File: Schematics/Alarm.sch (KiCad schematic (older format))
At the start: 7 parts, among them U8 BluetoothModule, U9 Arduino

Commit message: Fixed a layer
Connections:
- wire segments 37 -> 36
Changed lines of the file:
@@
 	4050 2800 4050 3400
 Wire Wire Line
-	7450 3400 7400 3400
-Wire Wire Line
 	6000 3400 6000 3300
-Connection ~ 7400 3400
-Wire Wire Line
-	7400 3400 6000 3400
 Wire Wire Line
 	5950 3400 5950 3500
@@
 Wire Wire Line
 	5050 3200 5650 3200
+Wire Wire Line
+	6000 3400 7400 3400
 $EndSCHEMATC

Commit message: Fixed repo
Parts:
- removed U9: Arduino, symbol CapstoneSchematic:Arduino
- added XA?: Arduino_Mega2560_Shield, symbol CapstoneSchematic:Arduino_Mega2560_Shield
- renumbered Alarm_Silence1 to Alarm_Silence, BZ1 to BZ?, D_RED2 to D_RED?, R4 to R?, U8 to U?, ULoRa2 to ULoRa?
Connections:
- wire segments 36 -> 56
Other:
- moved on the sheet: Alarm_Silence, BZ?, D_RED?, R?, U?, ULoRa?

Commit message: Made things look better on wireless alarm
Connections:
- net +5V: no longer XA?.5V3 (5V)
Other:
- note removed: "From USB Adapter"
- note removed: "Wireless Alarm Schematic"
- moved on the sheet: Alarm_Silence, BZ?, D_RED?, R?, ULoRa?

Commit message: Added Michael's alarm pcb rev
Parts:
- Alarm_Silence1: renamed from Alarm_Silence; footprint (none) -> Button_Switch_THT:SW_PUSH_6mm
- BZ1: renamed from BZ?; footprint (none) -> Buzzer_Beeper:Buzzer_15x7.5RM7.6
- D_RED1: renamed from D_RED?; footprint (none) -> LED_THT:LED_D5.0mm
- R1: renamed from R?; footprint (none) -> Resistor_THT:R_Axial_DIN0207_L6.3mm_D2.5mm_P2.54mm_Vertical
- U1: renamed from U?; footprint (none) -> Connector_PinSocket_2.54mm:PinSocket_1x04_P2.54mm_Horizontal
- ULoRa1: renamed from ULoRa?; footprint (none) -> Connector_PinSocket_2.54mm:PinSocket_1x06_P2.54mm_Horizontal
- XA1: renamed from XA?; footprint (none) -> Arduino:Arduino_Mega2560_Shield
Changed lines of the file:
@@
 EESchema Schematic File Version 4
-LIBS:CapstoneSchematic-cache
+LIBS:Alarm-cache
 EELAYER 30 0
 EELAYER END
 $Descr A4 11693 8268
 encoding utf-8
-Sheet 2 2
+Sheet 1 1
 Title "Wireless Alarm Schematic"
 Date ""
@@
 $EndDescr
 $Comp
-L power:GND #PWR?
+L power:GND #PWR0101
 U 1 1 5DC5496C
 P 11000 1800
-AR Path="/5DC5496C" Ref="#PWR?"  Part="1"
+AR Path="/5DC5496C" Ref="#PWR0101"  Part="1"
 AR Path="/5DC4244F/5DC5496C" Ref="#PWR0122"  Part="1"
-F 0 "#PWR0122" H 11000 1550 50  0001 C CNN
+F 0 "#PWR0101" H 11000 1550 50  0001 C CNN
 F 1 "GND" H 11005 1627 50  0000 C CNN
 F 2 "" H 11000 1800 50  0001 C CNN
@@
 $EndComp
 $Comp
-L Device:R R?
+L Device:R R1
 U 1 1 5DC54972
 P 10450 1800
-AR Path="/5DC54972" Ref="R?"  Part="1"
+AR Path="/5DC54972" Ref="R1"  Part="1"
 AR Path="/5DC4244F/5DC54972" Ref="R?"  Part="1"
-F 0 "R?" H 10380 1754 50  0000 R CNN
+F 0 "R1" H 10380 1754 50  0000 R CNN
 F 1 "220" H 10380 1845 50  0000 R CNN
-F 2 "" V 10380 1800 50  0001 C CNN
+F 2 "Resistor_THT:R_Axial_DIN0207_L6.3mm_D2.5mm_P2.54mm_Vertical" V 10380 1800 50  0001 C CNN
 F 3 "~" H 10450 1800 50  0001 C CNN
 	1    10450 1800
@@
 $EndComp
 $Comp
-L power:GND #PWR?
+L power:GND #PWR0102
 U 1 1 5DC549DA
 P 4225 2825
-AR Path="/5DC549DA" Ref="#PWR?"  Part="1"
+AR Path="/5DC549DA" Ref="#PWR0102"  Part="1"
 AR Path="/5DC4244F/5DC549DA" Ref="#PWR0123"  Part="1"
-F 0 "#PWR0123" H 4225 2575 50  0001 C CNN
+F 0 "#PWR0102" H 4225 2575 50  0001 C CNN
 F 1 "GND" H 4230 2652 50  0000 C CNN
 F 2 "" H 4225 2825 50  0001 C CNN
@@
 $EndComp
 $Comp
-L power:+5V #PWR?
+L power:+5V #PWR0103
 U 1 1 5DC549E0
 P 4225 2325
-AR Path="/5DC549E0" Ref="#PWR?"  Part="1"
+AR Path="/5DC549E0" Ref="#PWR0103"  Part="1"
 AR Path="/5DC4244F/5DC549E0" Ref="#PWR0124"  Part="1"
-F 0 "#PWR0124" H 4225 2175 50  0001 C CNN
+F 0 "#PWR0103" H 4225 2175 50  0001 C CNN
 F 1 "+5V" H 4240 2498 50  0000 C CNN
 F 2 "" H 4225 2325 50  0001 C CNN
@@
 $EndComp
 $Comp
-L Device:LED D_RED?
+L Device:LED D_RED1
 U 1 1 5DC54A01
 P 10750 1800
-AR Path="/5DC54A01" Ref="D_RED?"  Part="1"
+AR Path="/5DC54A01" Ref="D_RED1"  Part="1"
 AR Path="/5DC4244F/5DC54A01" Ref="D_RED?"  Part="1"
-F 0 "D_RED?" H 10743 2016 50  0000 C CNN
+F 0 "D_RED1" H 10743 2016 50  0000 C CNN
 F 1 "LED" H 10743 1925 50  0000 C CNN
-F 2 "" H 10750 1800 50  0001 C CNN
+F 2 "LED_THT:LED_D5.0mm" H 10750 1800 50  0001 C CNN
 F 3 "~" H 10750 1800 50  0001 C CNN
 	1    10750 1800
@@
 	11000 1800 10900 1800
 $Comp
-L Device:Buzzer BZ?
+L Device:Buzzer BZ1
 U 1 1 5DC609D6
 P 10150 1225
-F 0 "BZ?" H 10156 900 50  0000 C CNN
+F 0 "BZ1" H 10156 900 50  0000 C CNN
 F 1 "Buzzer" H 10156 991 50  0000 C CNN
-F 2 "" V 10125 1325 50  0001 C CNN
+F 2 "Buzzer_Beeper:Buzzer_15x7.5RM7.6" V 10125 1325 50  0001 C CNN
 F 3 "~" V 10125 1325 50  0001 C CNN
 	1    10150 1225
@@
 $EndComp
 $Comp
-L power:GND #PWR?
+L power:GND #PWR0104
 U 1 1 5DC60A34
 P 10250 1125
-AR Path="/5DC60A34" Ref="#PWR?"  Part="1"
+AR Path="/5DC60A34" Ref="#PWR0104"  Part="1"
 AR Path="/5DC4244F/5DC60A34" Ref="#PWR0126"  Part="1"
-F 0 "#PWR0126" H 10250 875 50  0001 C CNN
+F 0 "#PWR0104" H 10250 875 50  0001 C CNN
 F 1 "GND" V 10255 997 50  0000 R CNN
 F 2 "" H 10250 1125 50  0001 C CNN
@@
 $EndComp
 $Comp
-L power:+5V #PWR?
+L power:+5V #PWR0105
 U 1 1 5DC69508
 P 4150 1800
-AR Path="/5DC69508" Ref="#PWR?"  Part="1"
+AR Path="/5DC69508" Ref="#PWR0105"  Part="1"
 AR Path="/5DC4244F/5DC69508" Ref="#PWR0128"  Part="1"
-F 0 "#PWR0128" H 4150 1650 50  0001 C CNN
+F 0 "#PWR0105" H 4150 1650 50  0001 C CNN
 F 1 "+5V" H 4165 1973 50  0000 C CNN
 F 2 "" H 4150 1800 50  0001 C CNN
@@
 $EndComp
 $Comp
-L power:GND #PWR?
+L power:GND #PWR0106
 U 1 1 5DC69FE6
 P 4150 2000
-AR Path="/5DC69FE6" Ref="#PWR?"  Part="1"
+AR Path="/5DC69FE6" Ref="#PWR0106"  Part="1"
 AR Path="/5DC4244F/5DC69FE6" Ref="#PWR0129"  Part="1"
-F 0 "#PWR0129" H 4150 1750 50  0001 C CNN
+F 0 "#PWR0106" H 4150 1750 50  0001 C CNN
 F 1 "GND" H 4155 1827 50  0000 C CNN
 F 2 "" H 4150 2000 50  0001 C CNN
@@
 11/1/2019
 $Comp
-L power:GND #PWR?
+L power:GND #PWR0107
 U 1 1 5E4A2B00
 P 6350 5000
-F 0 "#PWR?" H 6350 4750 50  0001 C CNN
+F 0 "#PWR0107" H 6350 4750 50  0001 C CNN
 F 1 "GND" H 6355 4827 50  0000 C CNN
 F 2 "" H 6350 5000 50  0001 C CNN
@@
 	9450 2100 9050 2100
 $Comp
-L CapstoneSchematic:LoRa ULoRa?
+L CapstoneSchematic:LoRa ULoRa1
 U 1 1 5DC549E8
 P 4125 2325
-AR Path="/5DC549E8" Ref="ULoRa?"  Part="1"
+AR Path="/5DC549E8" Ref="ULoRa1"  Part="1"
 AR Path="/5DC4244F/5DC549E8" Ref="ULoRa?"  Part="1"
-F 0 "ULoRa?" H 5503 2271 50  0000 L CNN
+F 0 "ULoRa1" H 5503 2271 50  0000 L CNN
 F 1 "LoRa" H 5503 2180 50  0000 L CNN
-F 2 "" H 4675 2125 50  0001 C CNN
+F 2 "Connector_PinSocket_2.54mm:PinSocket_1x06_P2.54mm_Horizontal" H 4675 2125 50  0001 C CNN
 F 3 "" H 4675 2125 50  0001 C CNN
 	1    4125 2325
@@
 $EndComp
 $Comp
-L CapstoneSchematic:BluetoothModule U?
+L CapstoneSchematic:BluetoothModule U1
 U 1 1 5DC67D77
 P 4050 1500
-F 0 "U?" H 4294 885 50  0000 C CNN
+F 0 "U1" H 4294 885 50  0000 C CNN
 F 1 "BluetoothModule" H 4294 976 50  0000 C CNN
-F 2 "" H 4350 1000 50  0001 C CNN
+F 2 "Connector_PinSocket_2.54mm:PinSocket_1x04_P2.54mm_Horizontal" H 4350 1000 50  0001 C CNN
 F 3 "" H 4350 1000 50  0001 C CNN
 	1    4050 1500
@@
 $EndComp
 $Comp
-L CapstoneSchematic:Arduino_Mega2560_Shield XA?
+L CapstoneSchematic:Arduino_Mega2560_Shield XA1
 U 1 1 5E49C0DD
 P 7750 3750
-F 0 "XA?" H 7750 1370 60  0000 C CNN
+F 0 "XA1" H 7750 1370 60  0000 C CNN
 F 1 "Arduino_Mega2560_Shield" H 7750 1264 60  0000 C CNN
-F 2 "" H 8450 6500 60  0001 C CNN
+F 2 "Arduino:Arduino_Mega2560_Shield" H 8450 6500 60  0001 C CNN
 F 3 "https://store.arduino.cc/arduino-mega-2560-rev3" H 8450 6500 60  0001 C CNN
 	1    7750 3750
@@
 $EndComp
 $Comp
-L power:+5V #PWR?
+L power:+5V #PWR0108
 U 1 1 5DC6E068
 P 10200 2425
-AR Path="/5DC6E068" Ref="#PWR?"  Part="1"
+AR Path="/5DC6E068" Ref="#PWR0108"  Part="1"
 AR Path="/5DC4244F/5DC6E068" Ref="#PWR0130"  Part="1"
-F 0 "#PWR0130" H 10200 2275 50  0001 C CNN
+F 0 "#PWR0108" H 10200 2275 50  0001 C CNN
 F 1 "+5V" H 10215 2598 50  0000 C CNN
 F 2 "" H 10200 2425 50  0001 C CNN
@@
 $EndComp
 $Comp
-L Switch:SW_MEC_5G Alarm_Silence
-U 1 1 5DC6DC68
-P 9925 2425
-F 0 "Alarm_Silence" H 9925 2710 50  0000 C CNN
-F 1 "SW_MEC_5G" H 9925 2619 50  0000 C CNN
-F 2 "" H 9925 2625 50  0001 C CNN
-F 3 "http://www.apem.com/int/index.php?controller=attachment&id_attachment=488" H 9925 2625 50  0001 C CNN
-	1    9925 2425
-	-1   0    0    -1
-$EndComp
-$Comp
-L power:+5V #PWR?
+L power:+5V #PWR0109
 U 1 1 5E54092B
 P 6350 5600
-F 0 "#PWR?" H 6350 5450 50  0001 C CNN
+F 0 "#PWR0109" H 6350 5450 50  0001 C CNN
 F 1 "+5V" H 6365 5773 50  0000 C CNN
 F 2 "" H 6350 5600 50  0001 C CNN
@@
 Wire Wire Line
 	9450 2425 9725 2425
+$Comp
+L Switch:SW_MEC_5G Alarm_Silence1
+U 1 1 5DC6DC68
+P 9925 2425
+F 0 "Alarm_Silence1" H 9925 2710 50  0000 C CNN
+F 1 "SW_MEC_5G" H 9925 2619 50  0000 C CNN
+F 2 "Button_Switch_THT:SW_PUSH_6mm" H 9925 2625 50  0001 C CNN
+F 3 "http://www.apem.com/int/index.php?controller=attachment&id_attachment=488" H 9925 2625 50  0001 C CNN
+	1    9925 2425
+	-1   0    0    -1
+$EndComp
 $EndSCHEMATC

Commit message: Fixed button
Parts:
- removed Alarm_Silence1: SW_MEC_5G, Button_Switch_THT:SW_PUSH_6mm, symbol Switch:SW_MEC_5G
- removed D_RED1: LED, LED_THT:LED_D5.0mm, symbol Device:LED
- removed R1: 220, Resistor_THT:R_Axial_DIN0207_L6.3mm_D2.5mm_P2.54mm_Vertical, symbol Device:R
- added SW?: SW_MEC_5G_LED, symbol Switch:SW_MEC_5G_LED
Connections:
- net GND: now also SW?.1, SW?.2
- net at XA1.D7: now also SW?.3 (K)
- net at XA1.D8: now also SW?.4 (A)
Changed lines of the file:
@@
 EESchema Schematic File Version 4
-LIBS:CapstoneSchematic-cache
+LIBS:Alarm-cache
 EELAYER 30 0
 EELAYER END
 $Descr A4 11693 8268
 encoding utf-8
-Sheet 1 2
+Sheet 1 1
 Title "Wireless Alarm Schematic"
 Date ""
@@
 Comment4 ""
 $EndDescr
-$Comp
-L power:GND #PWR0101
-U 1 1 5DC5496C
-P 11000 1800
-AR Path="/5DC5496C" Ref="#PWR0101"  Part="1"
-AR Path="/5DC4244F/5DC5496C" Ref="#PWR0122"  Part="1"
-F 0 "#PWR0101" H 11000 1550 50  0001 C CNN
-F 1 "GND" H 11005 1627 50  0000 C CNN
-F 2 "" H 11000 1800 50  0001 C CNN
-F 3 "" H 11000 1800 50  0001 C CNN
-	1    11000 1800
-	0    -1   -1   0
-$EndComp
-$Comp
-L Device:R R1
-U 1 1 5DC54972
-P 10450 1800
-AR Path="/5DC54972" Ref="R1"  Part="1"
-AR Path="/5DC4244F/5DC54972" Ref="R?"  Part="1"
-F 0 "R1" H 10380 1754 50  0000 R CNN
-F 1 "220" H 10380 1845 50  0000 R CNN
-F 2 "Resistor_THT:R_Axial_DIN0207_L6.3mm_D2.5mm_P2.54mm_Vertical" V 10380 1800 50  0001 C CNN
-F 3 "~" H 10450 1800 50  0001 C CNN
-	1    10450 1800
-	0    -1   -1   0
-$EndComp
 $Comp
 L power:GND #PWR0102
@@
 $EndComp
 $Comp
-L Device:LED D_RED1
-U 1 1 5DC54A01
-P 10750 1800
-AR Path="/5DC54A01" Ref="D_RED1"  Part="1"
-AR Path="/5DC4244F/5DC54A01" Ref="D_RED?"  Part="1"
-F 0 "D_RED1" H 10743 2016 50  0000 C CNN
-F 1 "LED" H 10743 1925 50  0000 C CNN
-F 2 "LED_THT:LED_D5.0mm" H 10750 1800 50  0001 C CNN
-F 3 "~" H 10750 1800 50  0001 C CNN
-	1    10750 1800
-	-1   0    0    -1
-$EndComp
-Wire Wire Line
-	11000 1800 10900 1800
-$Comp
 L Device:Buzzer BZ1
 U 1 1 5DC609D6
@@
 Wire Wire Line
 	4675 2425 4225 2425
-Text GLabel 9600 2000 2    50   Input ~ 0
-Lora_Reset
 Wire Wire Line
 	6450 1600 4150 1600
@@
 	9600 2000 9050 2000
 Wire Wire Line
-	9450 2100 9050 2100
+	9450 2200 9050 2200
 $Comp
 L CapstoneSchematic:LoRa ULoRa1
@@
 $EndComp
 $Comp
-L power:+5V #PWR0108
-U 1 1 5DC6E068
-P 10200 2425
-AR Path="/5DC6E068" Ref="#PWR0108"  Part="1"
-AR Path="/5DC4244F/5DC6E068" Ref="#PWR0130"  Part="1"
-F 0 "#PWR0108" H 10200 2275 50  0001 C CNN
-F 1 "+5V" H 10215 2598 50  0000 C CNN
-F 2 "" H 10200 2425 50  0001 C CNN
-F 3 "" H 10200 2425 50  0001 C CNN
-	1    10200 2425
-	0    1    -1   0
-$EndComp
-$Comp
 L power:+5V #PWR0109
 U 1 1 5E54092B
@@
 	6350 5600 6450 5600
 Wire Wire Line
-	9050 1800 10300 1800
-Wire Wire Line
 	9750 1100 10050 1100
 Wire Wire Line
@@
 	5400 1900 5400 2625
 Wire Wire Line
-	10125 2425 10200 2425
-Wire Wire Line
-	9450 2100 9450 2425
+	10125 2425 10150 2425
+Text GLabel 9600 2000 2    50   Input ~ 0
+Lora_Reset
+$Comp
+L Switch:SW_MEC_5G_LED SW?
+U 1 1 5E936E97
+P 9925 2325
+F 0 "SW?" H 9925 2710 50  0000 C CNN
+F 1 "SW_MEC_5G_LED" H 9925 2619 50  0000 C CNN
+F 2 "" H 9925 2625 50  0001 C CNN
+F 3 "http://www.apem.com/int/index.php?controller=attachment&id_attachment=488" H 9925 2625 50  0001 C CNN
+	1    9925 2325
+	-1   0    0    1
+$EndComp
+Wire Wire Line
+	10125 2325 10150 2325
+Wire Wire Line
+	10150 2325 10150 2425
+Connection ~ 10150 2425
+Wire Wire Line
+	10150 2425 10200 2425
+$Comp
+L power:GND #PWR?
+U 1 1 5E944770
+P 10200 2425
+F 0 "#PWR?" H 10200 2175 50  0001 C CNN
+F 1 "GND" V 10205 2297 50  0000 R CNN
+F 2 "" H 10200 2425 50  0001 C CNN
+F 3 "" H 10200 2425 50  0001 C CNN
+	1    10200 2425
+	0    -1   -1   0
+$EndComp
 Wire Wire Line
 	9450 2425 9725 2425
-$Comp
-L Switch:SW_MEC_5G Alarm_Silence1
-U 1 1 5DC6DC68
-P 9925 2425
-F 0 "Alarm_Silence1" H 9925 2710 50  0000 C CNN
-F 1 "SW_MEC_5G" H 9925 2619 50  0000 C CNN
-F 2 "Button_Switch_THT:SW_PUSH_6mm" H 9925 2625 50  0001 C CNN
-F 3 "http://www.apem.com/int/index.php?controller=attachment&id_attachment=488" H 9925 2625 50  0001 C CNN
-	1    9925 2425
-	-1   0    0    -1
-$EndComp
+Wire Wire Line
+	9725 2325 9650 2325
+Wire Wire Line
+	9450 2200 9450 2425
+Wire Wire Line
+	9650 2325 9650 2100
+Wire Wire Line
+	9650 2100 9050 2100
 $EndSCHEMATC

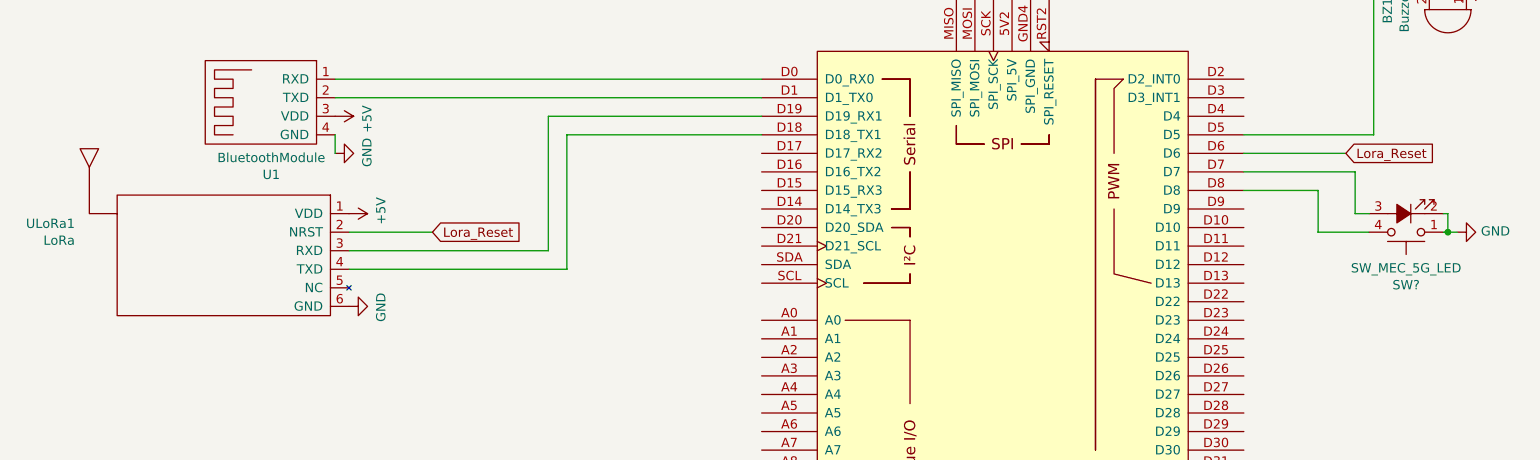
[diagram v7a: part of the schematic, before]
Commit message: Fixed most of schematic, need to update linear regulator footprint
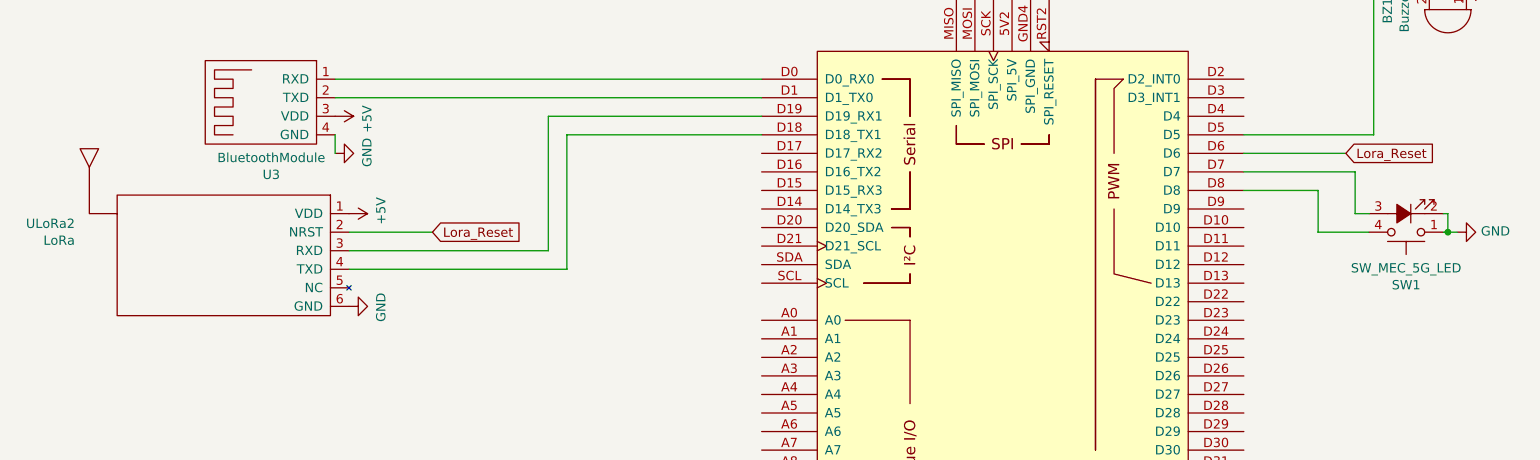
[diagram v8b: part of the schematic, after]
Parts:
- gave numbers to parts that had none: 1
- renumbered U1 to U3, ULoRa1 to ULoRa2
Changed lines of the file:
@@
 EESchema Schematic File Version 4
-LIBS:Alarm-cache
+LIBS:CapstoneSchematic-cache
 EELAYER 30 0
 EELAYER END
 $Descr A4 11693 8268
 encoding utf-8
-Sheet 1 1
+Sheet 2 2
 Title "Wireless Alarm Schematic"
 Date ""
@@
 $EndDescr
 $Comp
-L power:GND #PWR0102
+L power:GND #PWR?
 U 1 1 5DC549DA
 P 4225 2825
-AR Path="/5DC549DA" Ref="#PWR0102"  Part="1"
-AR Path="/5DC4244F/5DC549DA" Ref="#PWR0123"  Part="1"
-F 0 "#PWR0102" H 4225 2575 50  0001 C CNN
+AR Path="/5DC549DA" Ref="#PWR?"  Part="1"
+AR Path="/5DC4244F/5DC549DA" Ref="#PWR033"  Part="1"
+F 0 "#PWR033" H 4225 2575 50  0001 C CNN
 F 1 "GND" H 4230 2652 50  0000 C CNN
 F 2 "" H 4225 2825 50  0001 C CNN
@@
 $EndComp
 $Comp
-L power:+5V #PWR0103
+L power:+5V #PWR?
 U 1 1 5DC549E0
 P 4225 2325
-AR Path="/5DC549E0" Ref="#PWR0103"  Part="1"
-AR Path="/5DC4244F/5DC549E0" Ref="#PWR0124"  Part="1"
-F 0 "#PWR0103" H 4225 2175 50  0001 C CNN
+AR Path="/5DC549E0" Ref="#PWR?"  Part="1"
+AR Path="/5DC4244F/5DC549E0" Ref="#PWR032"  Part="1"
+F 0 "#PWR032" H 4225 2175 50  0001 C CNN
 F 1 "+5V" H 4240 2498 50  0000 C CNN
 F 2 "" H 4225 2325 50  0001 C CNN
@@
 $EndComp
 $Comp
-L power:GND #PWR0104
+L power:GND #PWR?
 U 1 1 5DC60A34
 P 10250 1125
-AR Path="/5DC60A34" Ref="#PWR0104"  Part="1"
-AR Path="/5DC4244F/5DC60A34" Ref="#PWR0126"  Part="1"
-F 0 "#PWR0104" H 10250 875 50  0001 C CNN
+AR Path="/5DC60A34" Ref="#PWR?"  Part="1"
+AR Path="/5DC4244F/5DC60A34" Ref="#PWR037"  Part="1"
+F 0 "#PWR037" H 10250 875 50  0001 C CNN
 F 1 "GND" V 10255 997 50  0000 R CNN
 F 2 "" H 10250 1125 50  0001 C CNN
@@
 $EndComp
 $Comp
-L power:+5V #PWR0105
+L power:+5V #PWR?
 U 1 1 5DC69508
 P 4150 1800
-AR Path="/5DC69508" Ref="#PWR0105"  Part="1"
-AR Path="/5DC4244F/5DC69508" Ref="#PWR0128"  Part="1"
-F 0 "#PWR0105" H 4150 1650 50  0001 C CNN
+AR Path="/5DC69508" Ref="#PWR?"  Part="1"
+AR Path="/5DC4244F/5DC69508" Ref="#PWR030"  Part="1"
+F 0 "#PWR030" H 4150 1650 50  0001 C CNN
 F 1 "+5V" H 4165 1973 50  0000 C CNN
 F 2 "" H 4150 1800 50  0001 C CNN
@@
 $EndComp
 $Comp
-L power:GND #PWR0106
+L power:GND #PWR?
 U 1 1 5DC69FE6
 P 4150 2000
-AR Path="/5DC69FE6" Ref="#PWR0106"  Part="1"
-AR Path="/5DC4244F/5DC69FE6" Ref="#PWR0129"  Part="1"
-F 0 "#PWR0106" H 4150 1750 50  0001 C CNN
+AR Path="/5DC69FE6" Ref="#PWR?"  Part="1"
+AR Path="/5DC4244F/5DC69FE6" Ref="#PWR031"  Part="1"
+F 0 "#PWR031" H 4150 1750 50  0001 C CNN
 F 1 "GND" H 4155 1827 50  0000 C CNN
 F 2 "" H 4150 2000 50  0001 C CNN
@@
 11/1/2019
 $Comp
-L power:GND #PWR0107
+L power:GND #PWR034
 U 1 1 5E4A2B00
 P 6350 5000
-F 0 "#PWR0107" H 6350 4750 50  0001 C CNN
+F 0 "#PWR034" H 6350 4750 50  0001 C CNN
 F 1 "GND" H 6355 4827 50  0000 C CNN
 F 2 "" H 6350 5000 50  0001 C CNN
@@
 	9450 2200 9050 2200
 $Comp
-L CapstoneSchematic:LoRa ULoRa1
+L CapstoneSchematic:LoRa ULoRa?
 U 1 1 5DC549E8
 P 4125 2325
-AR Path="/5DC549E8" Ref="ULoRa1"  Part="1"
-AR Path="/5DC4244F/5DC549E8" Ref="ULoRa?"  Part="1"
-F 0 "ULoRa1" H 5503 2271 50  0000 L CNN
+AR Path="/5DC549E8" Ref="ULoRa?"  Part="1"
+AR Path="/5DC4244F/5DC549E8" Ref="ULoRa2"  Part="1"
+F 0 "ULoRa2" H 5503 2271 50  0000 L CNN
 F 1 "LoRa" H 5503 2180 50  0000 L CNN
 F 2 "Connector_PinSocket_2.54mm:PinSocket_1x06_P2.54mm_Horizontal" H 4675 2125 50  0001 C CNN
@@
 $EndComp
 $Comp
-L CapstoneSchematic:BluetoothModule U1
+L CapstoneSchematic:BluetoothModule U3
 U 1 1 5DC67D77
 P 4050 1500
-F 0 "U1" H 4294 885 50  0000 C CNN
+F 0 "U3" H 4294 885 50  0000 C CNN
 F 1 "BluetoothModule" H 4294 976 50  0000 C CNN
 F 2 "Connector_PinSocket_2.54mm:PinSocket_1x04_P2.54mm_Horizontal" H 4350 1000 50  0001 C CNN
@@
 $EndComp
 $Comp
-L power:+5V #PWR0109
+L power:+5V #PWR035
 U 1 1 5E54092B
 P 6350 5600
-F 0 "#PWR0109" H 6350 5450 50  0001 C CNN
+F 0 "#PWR035" H 6350 5450 50  0001 C CNN
 F 1 "+5V" H 6365 5773 50  0000 C CNN
 F 2 "" H 6350 5600 50  0001 C CNN
@@
 Lora_Reset
 $Comp
-L Switch:SW_MEC_5G_LED SW?
+L Switch:SW_MEC_5G_LED SW1
 U 1 1 5E936E97
 P 9925 2325
-F 0 "SW?" H 9925 2710 50  0000 C CNN
+F 0 "SW1" H 9925 2710 50  0000 C CNN
 F 1 "SW_MEC_5G_LED" H 9925 2619 50  0000 C CNN
 F 2 "" H 9925 2625 50  0001 C CNN
@@
 	10150 2425 10200 2425
 $Comp
-L power:GND #PWR?
+L power:GND #PWR036
 U 1 1 5E944770
 P 10200 2425
-F 0 "#PWR?" H 10200 2175 50  0001 C CNN
+F 0 "#PWR036" H 10200 2175 50  0001 C CNN
 F 1 "GND" V 10205 2297 50  0000 R CNN
 F 2 "" H 10200 2425 50  0001 C CNN
